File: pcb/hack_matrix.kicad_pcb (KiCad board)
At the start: 11 copper layers, 30.9 x 26.7 mm, 16 parts, among them J1 USB_C_Receptacle_USB2.0_16P, J2 Screw_Terminal_01x02, SW2 SW_Push, U1 SN74AHCT245PWR, U3 XC6206P332MR, U4 ESP32-S2-MINI-2, U5 SN74AHCT245PWR

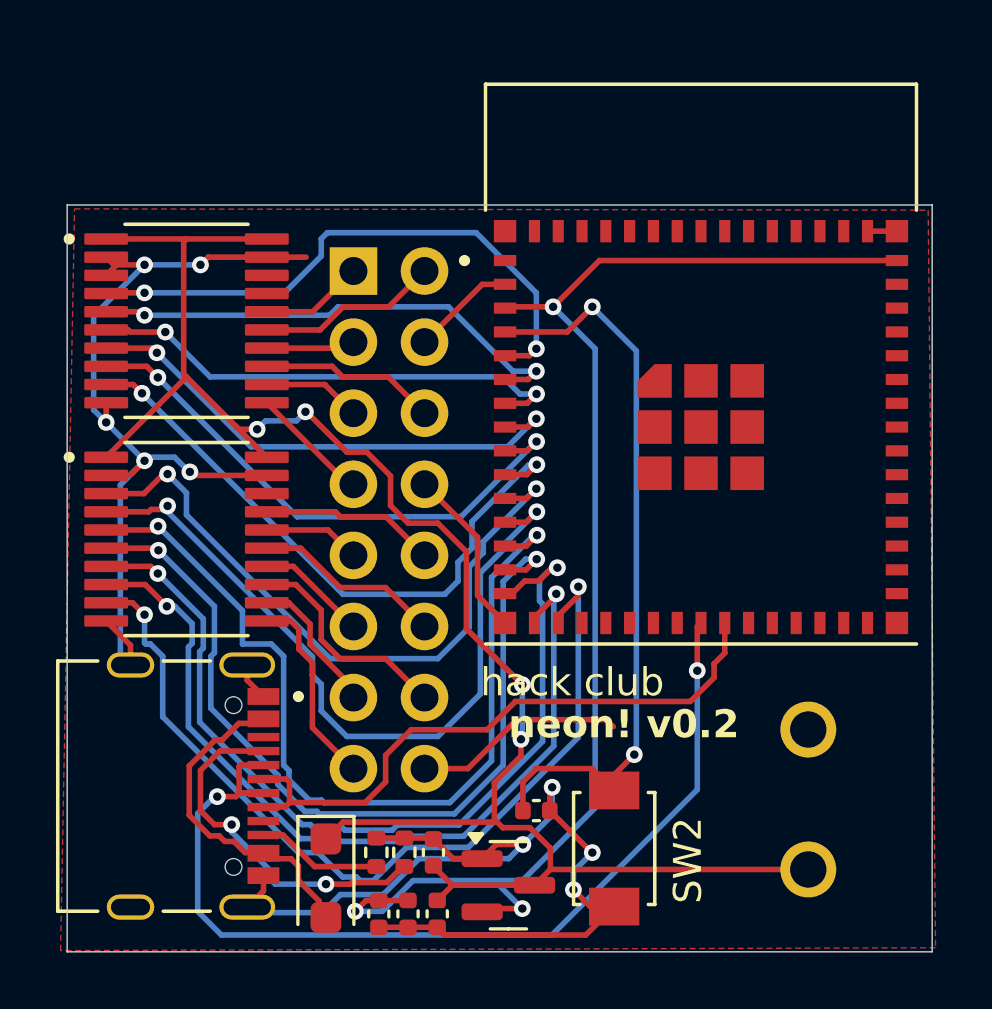
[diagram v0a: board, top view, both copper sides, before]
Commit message: esp32-s2 -> esp32-s3
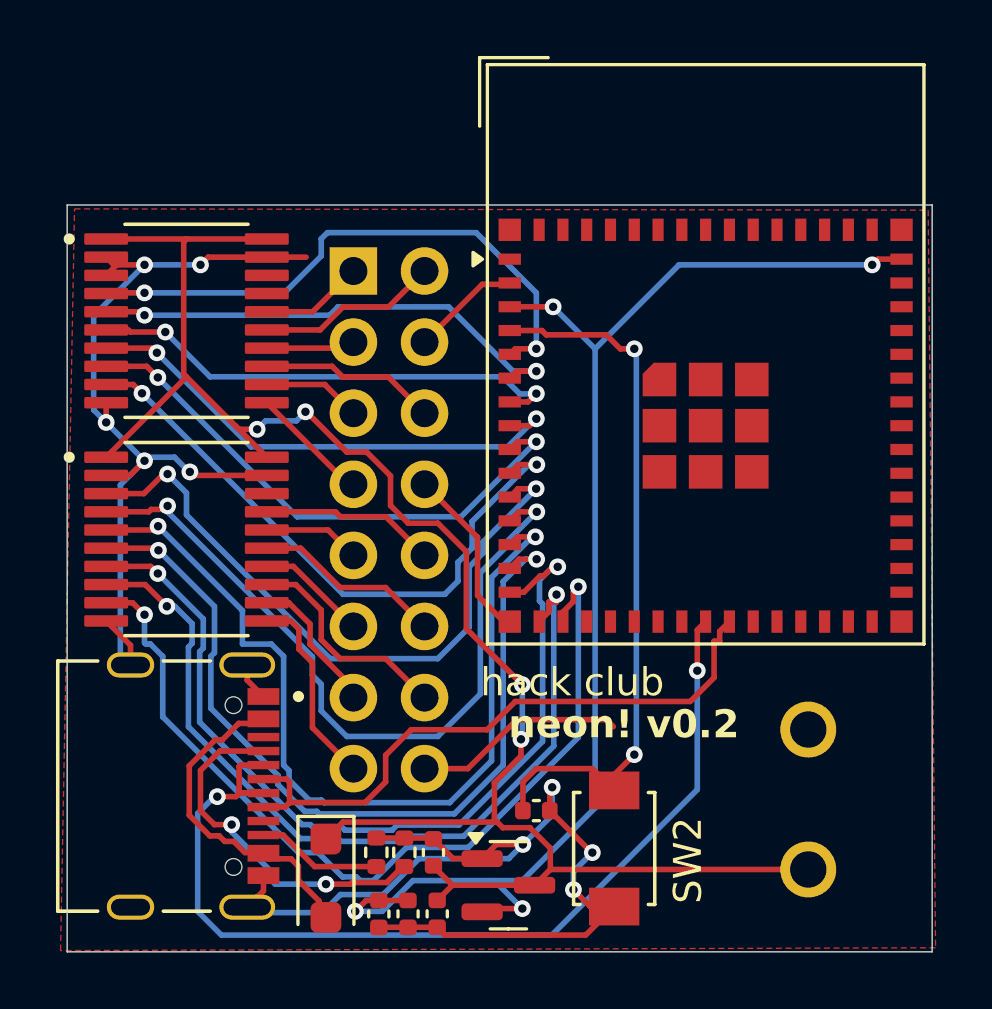
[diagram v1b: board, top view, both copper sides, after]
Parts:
- removed U4: ESP32-S2-MINI-2, ESP32-S2-MINI-2:XCVR_ESP32-S2-MINI-2
- added U6: ESP32-S3-MINI-1-N8, RF_Module:ESP32-S2-MINI-1, F.Cu at (189.5, 72.2)
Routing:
- net /GPIO0: track 26.5 -> 25.7 mm
- net +3V3: track 48.2 -> 47.4 mm, vias 3 -> 4
- net GND: track 88.8 -> 88.1 mm
